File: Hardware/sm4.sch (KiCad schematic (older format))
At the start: 93 parts, among them J1 Motor1, J2 Termination, J3 CAN bus, J4 Motor2, J5 I2C, J6 Power, J7 USB_C_Receptacle_USB2.0, J8 Conn_01x05_Male, Q1 NDT2955, SW1 RST_SW, SW2 BOOT_SW, U1 STM32F405RGTx, U2 TMC2100-TA, U3 MCP2562-E-SN, U4 TMC2100-TA, U6 MCP1700-3302E_SOT23, U7 USBLC6-2SC6, Y1 25 MHz

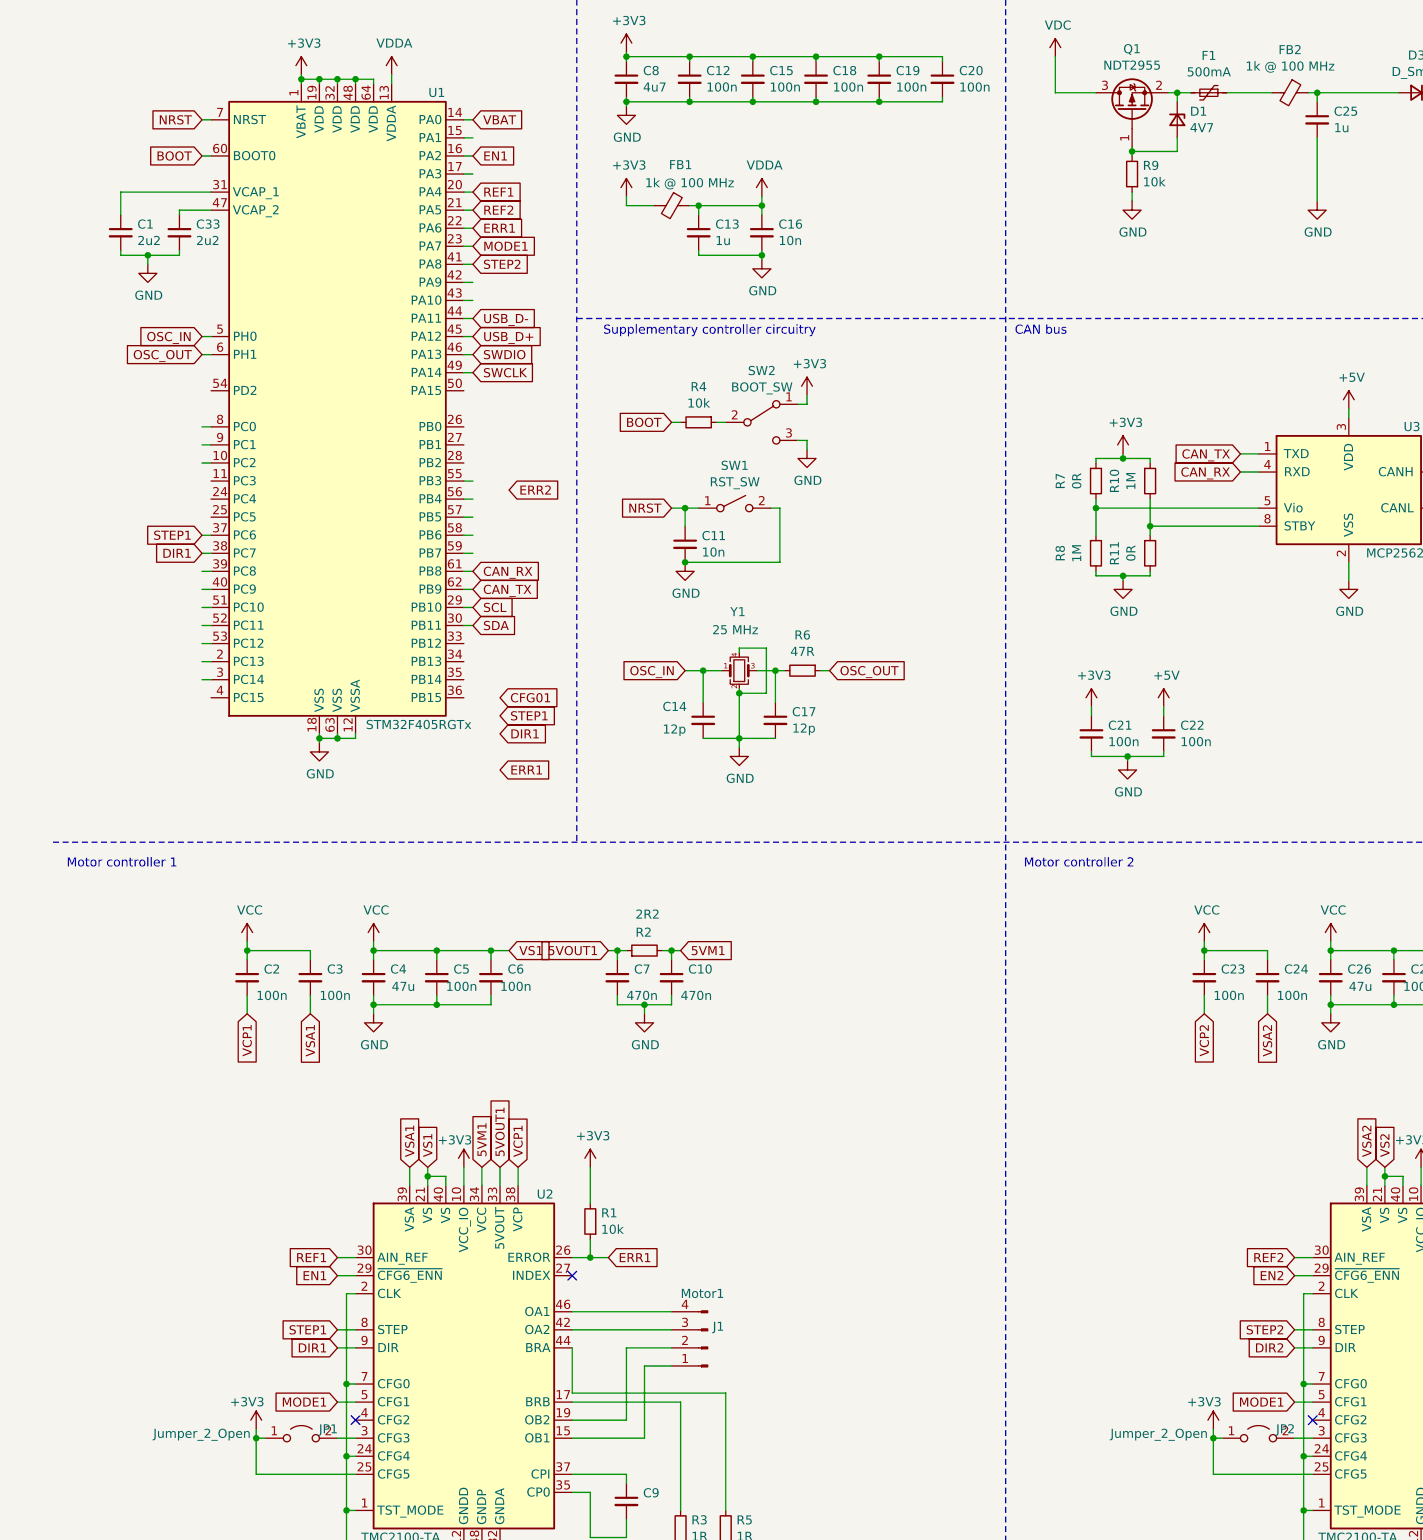
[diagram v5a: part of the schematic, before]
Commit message: Implement more of the second version of the PCB.
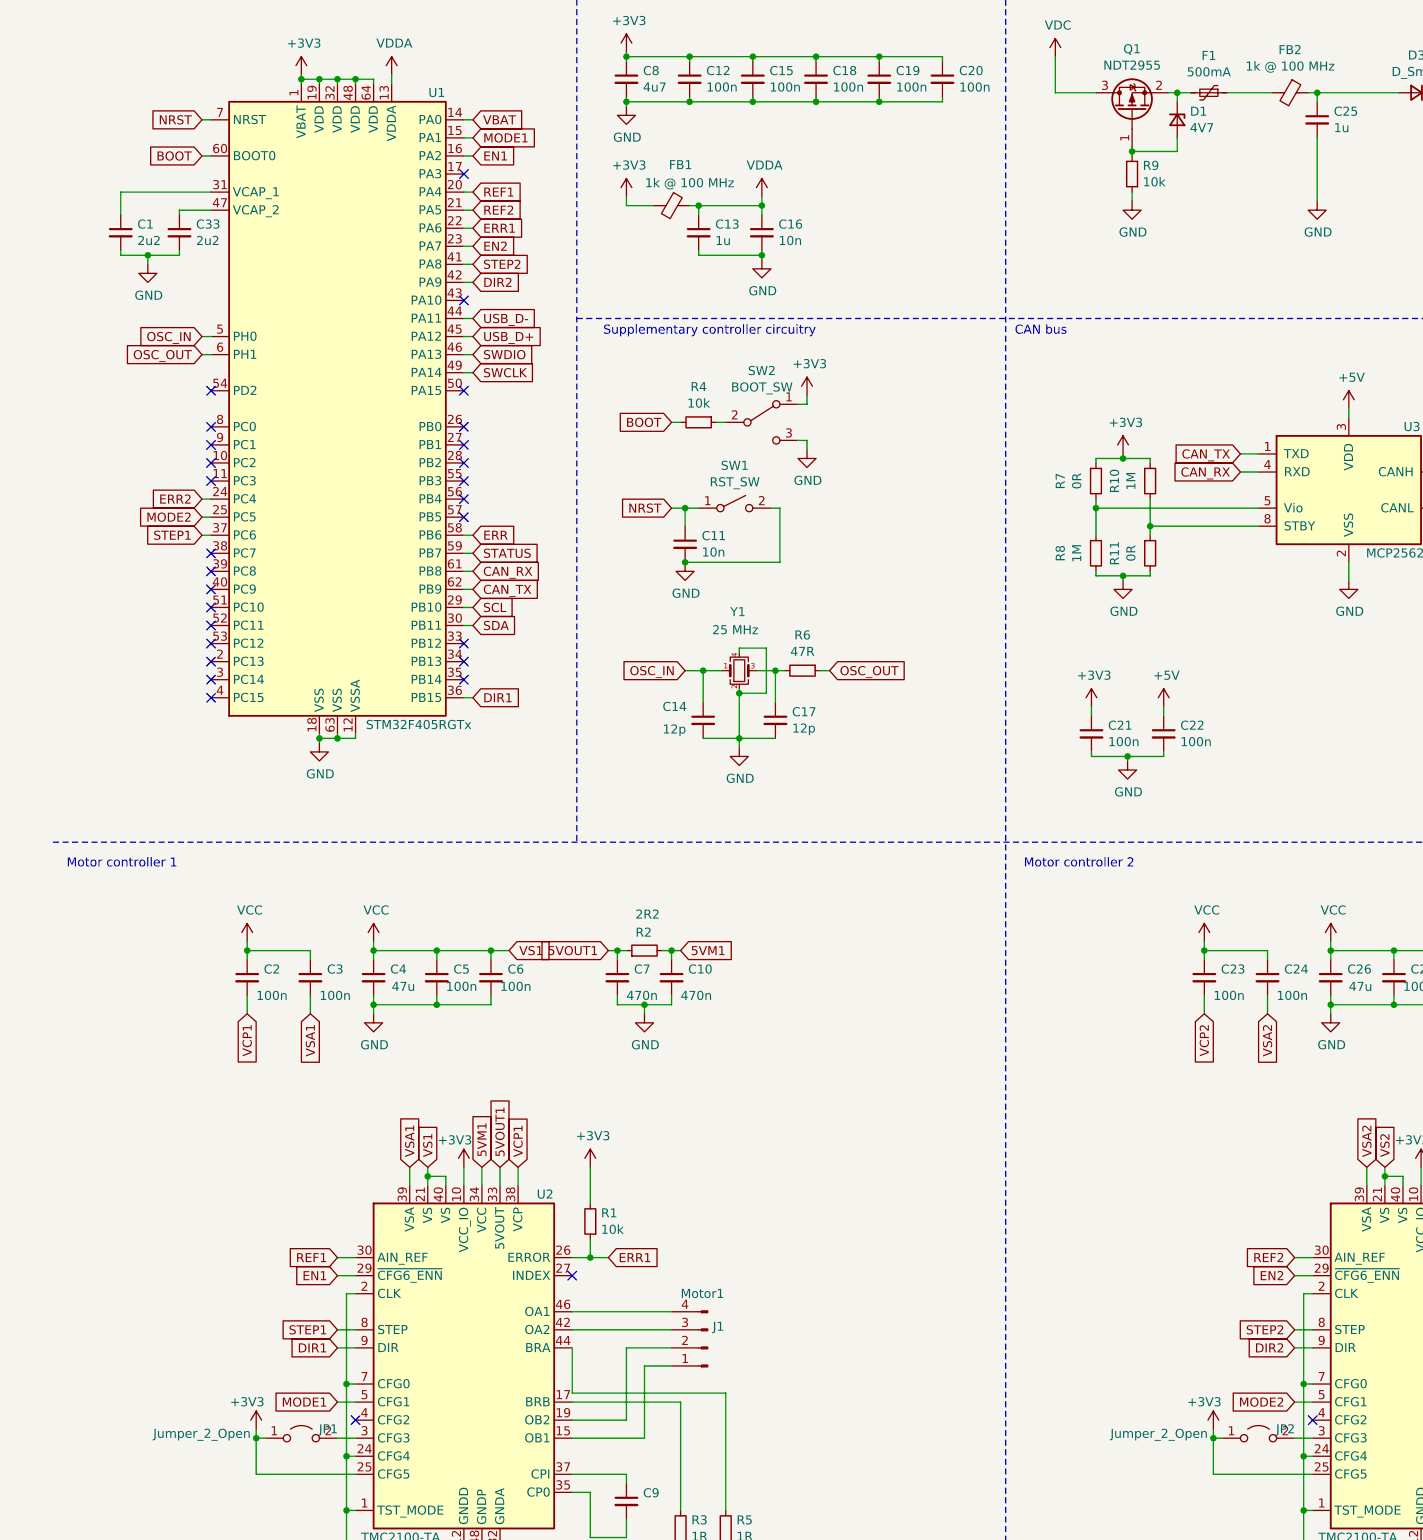
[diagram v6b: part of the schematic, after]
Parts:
- C10, C30, C31, C32, C7, C9: footprint Capacitor_SMD:C_0603_1608Metric_Pad1.08x0.95mm_HandSolder -> Capacitor_SMD:C_0402_1005Metric_Pad0.74x0.62mm_HandSolder
- C2, C23, C24, C28, C29, C3, C5, C6: footprint Capacitor_SMD:C_0805_2012Metric_Pad1.18x1.45mm_HandSolder -> Capacitor_SMD:C_0603_1608Metric_Pad1.08x0.95mm_HandSolder
- R14, R15, R2, R9: footprint Resistor_SMD:R_0603_1608Metric_Pad0.98x0.95mm_HandSolder -> Resistor_SMD:R_0402_1005Metric_Pad0.72x0.64mm_HandSolder
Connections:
- net labels added: MODE2
- net labels removed: CFG01
- wire segments 454 -> 441
- no-connect marks 6 -> 32
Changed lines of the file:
@@
 F 0 "R9" H 6391 1554 50  0000 R CNN
 F 1 "10k" H 6391 1645 50  0000 R CNN
-F 2 "Resistor_SMD:R_0603_1608Metric_Pad0.98x0.95mm_HandSolder" H 6450 1600 50  0001 C CNN
+F 2 "Resistor_SMD:R_0402_1005Metric_Pad0.72x0.64mm_HandSolder" H 6450 1600 50  0001 C CNN
 F 3 "~" H 6450 1600 50  0001 C CNN
 	1    6450 1600
@@
 F 0 "C2" H 1642 6096 50  0000 L CNN
 F 1 "100n" H 1600 5950 50  0000 L CNN
-F 2 "Capacitor_SMD:C_0805_2012Metric_Pad1.18x1.45mm_HandSolder" H 1550 6050 50  0001 C CNN
+F 2 "Capacitor_SMD:C_0603_1608Metric_Pad1.08x0.95mm_HandSolder" H 1550 6050 50  0001 C CNN
 F 3 "~" H 1550 6050 50  0001 C CNN
 	1    1550 6050
@@
 F 0 "C9" H 3742 8996 50  0000 L CNN
 F 1 "22n@50V" H 3450 8700 50  0000 L CNN
-F 2 "Capacitor_SMD:C_0603_1608Metric_Pad1.08x0.95mm_HandSolder" H 3650 8950 50  0001 C CNN
+F 2 "Capacitor_SMD:C_0402_1005Metric_Pad0.74x0.62mm_HandSolder" H 3650 8950 50  0001 C CNN
 F 3 "~" H 3650 8950 50  0001 C CNN
 	1    3650 8950
@@
 F 0 "C5" H 2692 6096 50  0000 L CNN
 F 1 "100n" H 2650 6000 50  0000 L CNN
-F 2 "Capacitor_SMD:C_0805_2012Metric_Pad1.18x1.45mm_HandSolder" H 2600 6050 50  0001 C CNN
+F 2 "Capacitor_SMD:C_0603_1608Metric_Pad1.08x0.95mm_HandSolder" H 2600 6050 50  0001 C CNN
 F 3 "~" H 2600 6050 50  0001 C CNN
 	1    2600 6050
@@
 F 0 "C3" H 1992 6096 50  0000 L CNN
 F 1 "100n" H 1950 5950 50  0000 L CNN
-F 2 "Capacitor_SMD:C_0805_2012Metric_Pad1.18x1.45mm_HandSolder" H 1900 6050 50  0001 C CNN
+F 2 "Capacitor_SMD:C_0603_1608Metric_Pad1.08x0.95mm_HandSolder" H 1900 6050 50  0001 C CNN
 F 3 "~" H 1900 6050 50  0001 C CNN
 	1    1900 6050
@@
 F 0 "C6" H 2992 6096 50  0000 L CNN
 F 1 "100n" H 2950 6000 50  0000 L CNN
-F 2 "Capacitor_SMD:C_0805_2012Metric_Pad1.18x1.45mm_HandSolder" H 2900 6050 50  0001 C CNN
+F 2 "Capacitor_SMD:C_0603_1608Metric_Pad1.08x0.95mm_HandSolder" H 2900 6050 50  0001 C CNN
 F 3 "~" H 2900 6050 50  0001 C CNN
 	1    2900 6050
@@
 F 0 "R2" V 3850 5950 50  0000 R CNN
 F 1 "2R2" V 3950 5950 50  0000 R CNN
-F 2 "Resistor_SMD:R_0603_1608Metric_Pad0.98x0.95mm_HandSolder" H 3750 5900 50  0001 C CNN
+F 2 "Resistor_SMD:R_0402_1005Metric_Pad0.72x0.64mm_HandSolder" H 3750 5900 50  0001 C CNN
 F 3 "~" H 3750 5900 50  0001 C CNN
 	1    3750 5900
@@
 F 0 "C7" H 3692 6096 50  0000 L CNN
 F 1 "470n" H 3650 5950 50  0000 L CNN
-F 2 "Capacitor_SMD:C_0603_1608Metric_Pad1.08x0.95mm_HandSolder" H 3600 6050 50  0001 C CNN
+F 2 "Capacitor_SMD:C_0402_1005Metric_Pad0.74x0.62mm_HandSolder" H 3600 6050 50  0001 C CNN
 F 3 "~" H 3600 6050 50  0001 C CNN
 	1    3600 6050
@@
 F 0 "C10" H 3992 6096 50  0000 L CNN
 F 1 "470n" H 3950 5950 50  0000 L CNN
-F 2 "Capacitor_SMD:C_0603_1608Metric_Pad1.08x0.95mm_HandSolder" H 3900 6050 50  0001 C CNN
+F 2 "Capacitor_SMD:C_0402_1005Metric_Pad0.74x0.62mm_HandSolder" H 3900 6050 50  0001 C CNN
 F 3 "~" H 3900 6050 50  0001 C CNN
 	1    3900 6050
@@
 F 0 "C23" H 6942 6096 50  0000 L CNN
 F 1 "100n" H 6900 5950 50  0000 L CNN
-F 2 "Capacitor_SMD:C_0805_2012Metric_Pad1.18x1.45mm_HandSolder" H 6850 6050 50  0001 C CNN
+F 2 "Capacitor_SMD:C_0603_1608Metric_Pad1.08x0.95mm_HandSolder" H 6850 6050 50  0001 C CNN
 F 3 "~" H 6850 6050 50  0001 C CNN
 	1    6850 6050
@@
 F 0 "C31" H 9042 8996 50  0000 L CNN
 F 1 "22n@50V" H 8750 8700 50  0000 L CNN
-F 2 "Capacitor_SMD:C_0603_1608Metric_Pad1.08x0.95mm_HandSolder" H 8950 8950 50  0001 C CNN
+F 2 "Capacitor_SMD:C_0402_1005Metric_Pad0.74x0.62mm_HandSolder" H 8950 8950 50  0001 C CNN
 F 3 "~" H 8950 8950 50  0001 C CNN
 	1    8950 8950
@@
 F 0 "C28" H 7992 6096 50  0000 L CNN
 F 1 "100n" H 7950 6000 50  0000 L CNN
-F 2 "Capacitor_SMD:C_0805_2012Metric_Pad1.18x1.45mm_HandSolder" H 7900 6050 50  0001 C CNN
+F 2 "Capacitor_SMD:C_0603_1608Metric_Pad1.08x0.95mm_HandSolder" H 7900 6050 50  0001 C CNN
 F 3 "~" H 7900 6050 50  0001 C CNN
 	1    7900 6050
@@
 F 0 "R14" H 8691 7354 50  0000 R CNN
 F 1 "10k" H 8691 7445 50  0000 R CNN
-F 2 "Resistor_SMD:R_0603_1608Metric_Pad0.98x0.95mm_HandSolder" H 8750 7400 50  0001 C CNN
+F 2 "Resistor_SMD:R_0402_1005Metric_Pad0.72x0.64mm_HandSolder" H 8750 7400 50  0001 C CNN
 F 3 "~" H 8750 7400 50  0001 C CNN
 	1    8750 7400
@@
 EN2
 Text GLabel 7350 8400 0    50   Input ~ 0
-MODE1
+MODE2
 Wire Wire Line
 	7350 8400 7450 8400
@@
 F 0 "C24" H 7292 6096 50  0000 L CNN
 F 1 "100n" H 7250 5950 50  0000 L CNN
-F 2 "Capacitor_SMD:C_0805_2012Metric_Pad1.18x1.45mm_HandSolder" H 7200 6050 50  0001 C CNN
+F 2 "Capacitor_SMD:C_0603_1608Metric_Pad1.08x0.95mm_HandSolder" H 7200 6050 50  0001 C CNN
 F 3 "~" H 7200 6050 50  0001 C CNN
 	1    7200 6050
@@
 F 0 "C29" H 8292 6096 50  0000 L CNN
 F 1 "100n" H 8250 6000 50  0000 L CNN
-F 2 "Capacitor_SMD:C_0805_2012Metric_Pad1.18x1.45mm_HandSolder" H 8200 6050 50  0001 C CNN
+F 2 "Capacitor_SMD:C_0603_1608Metric_Pad1.08x0.95mm_HandSolder" H 8200 6050 50  0001 C CNN
 F 3 "~" H 8200 6050 50  0001 C CNN
 	1    8200 6050
@@
 F 0 "R15" V 9150 5950 50  0000 R CNN
 F 1 "2R2" V 9250 5950 50  0000 R CNN
-F 2 "Resistor_SMD:R_0603_1608Metric_Pad0.98x0.95mm_HandSolder" H 9050 5900 50  0001 C CNN
+F 2 "Resistor_SMD:R_0402_1005Metric_Pad0.72x0.64mm_HandSolder" H 9050 5900 50  0001 C CNN
 F 3 "~" H 9050 5900 50  0001 C CNN
 	1    9050 5900
@@
 F 0 "C30" H 8992 6096 50  0000 L CNN
 F 1 "470n" H 8950 5950 50  0000 L CNN
-F 2 "Capacitor_SMD:C_0603_1608Metric_Pad1.08x0.95mm_HandSolder" H 8900 6050 50  0001 C CNN
+F 2 "Capacitor_SMD:C_0402_1005Metric_Pad0.74x0.62mm_HandSolder" H 8900 6050 50  0001 C CNN
 F 3 "~" H 8900 6050 50  0001 C CNN
 	1    8900 6050
@@
 F 0 "C32" H 9292 6096 50  0000 L CNN
 F 1 "470n" H 9250 5950 50  0000 L CNN
-F 2 "Capacitor_SMD:C_0603_1608Metric_Pad1.08x0.95mm_HandSolder" H 9200 6050 50  0001 C CNN
+F 2 "Capacitor_SMD:C_0402_1005Metric_Pad0.74x0.62mm_HandSolder" H 9200 6050 50  0001 C CNN
 F 3 "~" H 9200 6050 50  0001 C CNN
 	1    9200 6050
@@
 Wire Wire Line
 	2800 2100 2750 2100
-Wire Wire Line
-	1300 3800 1350 3800
-Text GLabel 2950 4600 2    50   Input ~ 0
-STEP1
-Wire Wire Line
-	2800 3400 2750 3400
 Text GLabel 2800 2100 2    50   Input ~ 0
 STEP2
 Wire Wire Line
 	2800 3600 2750 3600
-Text GLabel 2950 4700 2    50   Input ~ 0
-DIR1
-Wire Wire Line
-	2800 3500 2750 3500
-Text GLabel 2950 4500 2    50   Input ~ 0
-CFG01
-Wire Wire Line
-	2800 3300 2750 3300
-Wire Wire Line
-	1300 4100 1350 4100
-Wire Wire Line
-	1300 4000 1350 4000
-Wire Wire Line
-	1300 3900 1350 3900
 Wire Wire Line
 	2750 2200 2800 2200
-Wire Wire Line
-	2750 2300 2800 2300
-Text GLabel 2950 4900 2    50   Input ~ 0
-ERR1
 Wire Wire Line
 	2800 3700 2750 3700
@@
 	12225 1750 12225 1550
 Wire Wire Line
-	1300 4200 1350 4200
-Wire Wire Line
-	1300 4300 1350 4300
-Wire Wire Line
-	1300 4400 1350 4400
-Wire Wire Line
-	1300 3000 1350 3000
-Wire Wire Line
-	1300 3100 1350 3100
-Wire Wire Line
-	1300 3200 1350 3200
-Wire Wire Line
 	2800 1400 2750 1400
 Wire Wire Line
@@
 Wire Wire Line
 	2800 1300 2750 1300
-Text GLabel 3000 3350 2    50   Input ~ 0
+Text GLabel 1300 3400 0    50   Input ~ 0
 ERR2
-Wire Wire Line
-	2800 1600 2750 1600
 $Comp
 L MCU_ST_STM32F4:STM32F405RGTx U1
@@
 $EndComp
 NoConn ~ 7450 8500
-Text GLabel 2800 2000 2    50   Input ~ 0
+Text GLabel 2800 1400 2    50   Input ~ 0
 MODE1
-Text GLabel 1300 3700 0    50   Input ~ 0
+Text GLabel 2800 4500 2    50   Input ~ 0
 DIR1
-Wire Wire Line
-	1300 3700 1350 3700
 Text GLabel 2800 4100 2    50   Input ~ 0
 SDA
@@
 Wire Wire Line
 	7475 1150 7925 1150
+Wire Wire Line
+	2800 4500 2750 4500
+Text GLabel 2800 2000 2    50   Input ~ 0
+EN2
+Wire Wire Line
+	1350 3400 1300 3400
+Text GLabel 1300 3500 0    50   Input ~ 0
+MODE2
+Wire Wire Line
+	1300 3500 1350 3500
+Text GLabel 2800 2200 2    50   Input ~ 0
+DIR2
+Text GLabel 2800 3700 2    50   Input ~ 0
+STATUS
+Text GLabel 2800 3600 2    50   Input ~ 0
+ERR
+NoConn ~ 2750 3500
+NoConn ~ 2750 3400
+NoConn ~ 2750 3300
+NoConn ~ 2750 3200
+NoConn ~ 2750 2800
+NoConn ~ 2750 2300
+NoConn ~ 2750 1600
+NoConn ~ 2750 4200
+NoConn ~ 2750 4300
+NoConn ~ 2750 4400
+NoConn ~ 1350 4500
+NoConn ~ 1350 3700
+NoConn ~ 1350 3800
+NoConn ~ 1350 3900
+NoConn ~ 1350 4000
+NoConn ~ 1350 4100
+NoConn ~ 1350 4200
+NoConn ~ 1350 4300
+NoConn ~ 1350 4400
+NoConn ~ 1350 3300
+NoConn ~ 1350 3200
+NoConn ~ 1350 3100
+NoConn ~ 1350 3000
+NoConn ~ 1350 2800
+NoConn ~ 2750 3000
+NoConn ~ 2750 3100
 $EndSCHEMATC

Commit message: Finalize first HW version. Update firmware project.
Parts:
- removed D1: 4V7, Diode_SMD:D_SOD-123, symbol Device:D_Zener_Small
- removed Q1: NDT2955, Package_TO_SOT_SMD:SOT-23, symbol Transistor_FET:AO3401A
- removed R9: 10k, Resistor_SMD:R_0402_1005Metric_Pad0.72x0.64mm_HandSolder, symbol Device:R_Small
- added C27, C37, C38, C39, C40, C41, C42, C43: 10u, Capacitor_SMD:C_1206_3216Metric_Pad1.33x1.80mm_HandSolder, symbol Device:C_Small
- added JP3, JP4: Jumper_2_Open, Jumper:SolderJumper-2_P1.3mm_Open_TrianglePad1.0x1.5mm, symbol Jumper:Jumper_2_Open
- added Q1: NDT2955, Package_TO_SOT_SMD:SOT-223-3_TabPin2, symbol Transistor_FET:ZXMP4A16G
- added R25, R26: 2k2, Resistor_SMD:R_0402_1005Metric_Pad0.72x0.64mm_HandSolder, symbol Device:R_Small
- C1, C33: LCSC (none) -> C23630
- C10, C32: LCSC (none) -> C47339
- C11: LCSC (none) -> C57112
- C12, C15, C18, C19, C20, C21, C22: LCSC (none) -> C1525
- C13, C34, C35: LCSC (none) -> C15849
- C14, C17: LCSC (none) -> C1547
- C16, C36: LCSC (none) -> C15195
- C2, C23, C24, C28, C29, C3, C5, C6: LCSC (none) -> C14663
- C25: LCSC (none) -> C1848
- C26, C4: value 47u -> 10u; footprint Capacitor_SMD:C_Elec_8x6.2 -> Capacitor_SMD:C_1206_3216Metric_Pad1.33x1.80mm_HandSolder; LCSC (none) -> C13585
- C30, C7: value 470n -> 4u7; footprint Capacitor_SMD:C_0402_1005Metric_Pad0.74x0.62mm_HandSolder -> Capacitor_SMD:C_0603_1608Metric_Pad1.08x0.95mm_HandSolder; LCSC (none) -> C19666
- C31, C9: LCSC (none) -> C1532
- C8: LCSC (none) -> C19666
- D3, D4: LCSC (none) -> C8598
- D5, D6, D7: LCSC (none) -> C72038
- F1, F2: LCSC (none) -> C70076
- R1, R14, R4: LCSC (none) -> C25744
- R11, R7: LCSC (none) -> C17168
- R12, R13, R6: LCSC (none) -> C23182
- R15, R2: LCSC (none) -> C25101
- R16, R17, R3, R5: LCSC (none) -> C20686
- R18: LCSC (none) -> C25741
- R19: LCSC (none) -> C25900
- R20, R21, R24: LCSC (none) -> C25879
- R22, R23: LCSC (none) -> C25905
- U1: LCSC (none) -> C15742
- U3: LCSC (none) -> C53609
- U6: LCSC (none) -> C39051
- U7: LCSC (none) -> C7519
- Y1: LCSC (none) -> C9006
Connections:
- net +3V3: now also R25.2, R26.2
- net DIR1: now also U1.15 (PA1); no longer U1.36 (PB15)
- net DIR2: now also U1.33 (PB12); no longer U1.42 (PA9)
- net EN1: now also U1.22 (PA6); no longer U1.16 (PA2)
- net ERR1: now also U1.25 (PC5); no longer U1.22 (PA6)
- net GND: now also C24.2, C3.2, C27.2, C37.2, C38.2, C39.2, C40.2, C41.2, C42.2, C43.2, Q1.1 (G)
- net MODE1: now also U1.17 (PA3); no longer U1.15 (PA1)
- net MODE2: now also U1.42 (PA9); no longer U1.25 (PC5)
- net SCL: now also JP4.2 (B)
- net SDA: now also JP3.2 (B)
- net VBAT: now also U1.27 (PB1); no longer U1.14 (PA0)
- net VCC: now also U2.39 (VSA), U4.39 (VSA), C27.1, C37.1, C38.1, C39.1, C40.1, C41.1, C42.1, C43.1
- net VDC: now also Q1.2 (D)
- net at F1.2: now also Q1.3 (S)
- removed net VSA1: C3.2, U2.39 (VSA)
- removed net VSA2: C24.2, U4.39 (VSA)
- new net: JP3.1 (A), R25.1
- new net: JP4.1 (A), R26.1
- no-connect marks 32 -> 29
